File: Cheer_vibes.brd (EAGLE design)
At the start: 18.7 x 18.2 mm, 8 parts, among them M1 MOTORSMD, Q1 500mA/300V

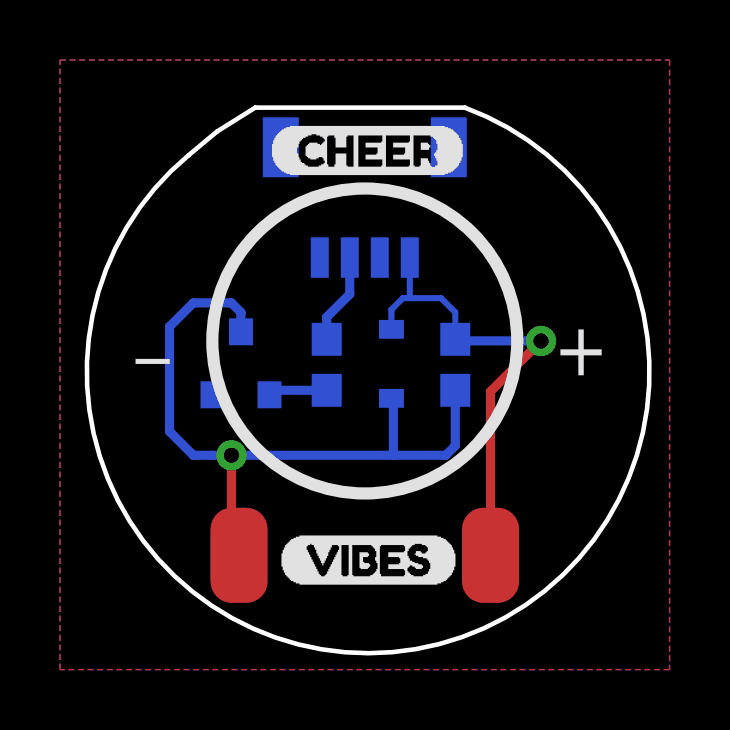
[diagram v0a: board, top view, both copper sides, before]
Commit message: Updating silk on vibe board
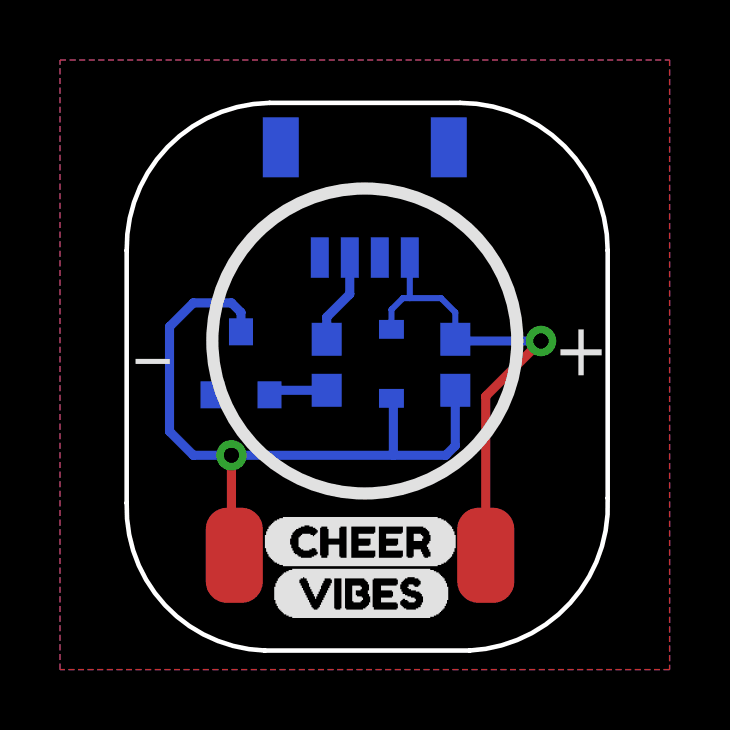
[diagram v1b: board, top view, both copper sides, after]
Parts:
- moved U$1 13.0 mm to (34.7, 32.2)
- moved U$2 1.14 mm to (35.0, 30.5)
- moved M1 0.16 mm to (37.9, 39.0)
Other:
- board size 18.7 x 18.2 mm -> 16 x 18.3 mm
